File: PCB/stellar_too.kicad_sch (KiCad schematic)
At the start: 8 parts, among them J1 USB_C_Receptacle_USB2.0_14P, J2 USB_C_Receptacle_USB2.0_16P, U1 MDBT50Q, U2 FUSB302B01MPX

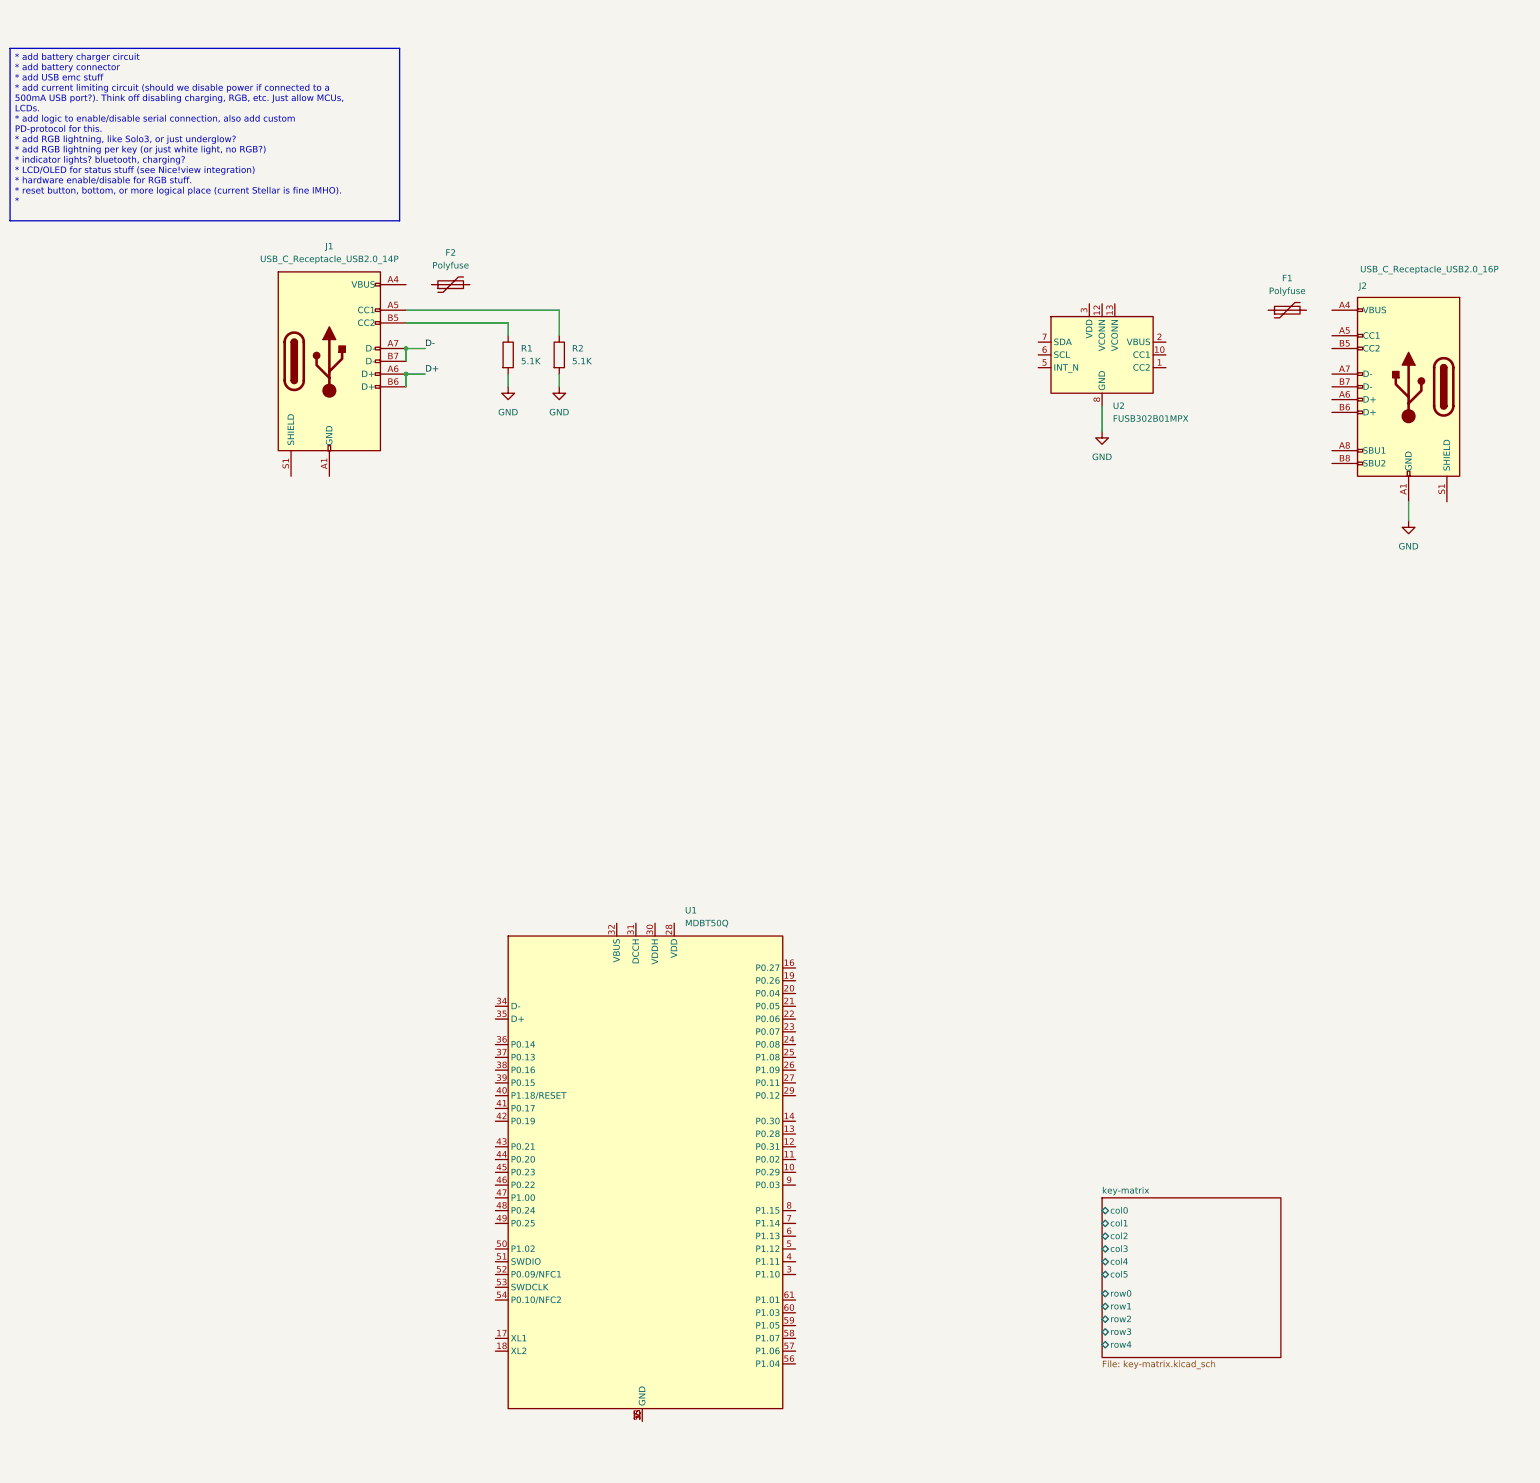
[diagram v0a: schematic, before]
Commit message: feat(pcb) layout of keys changed
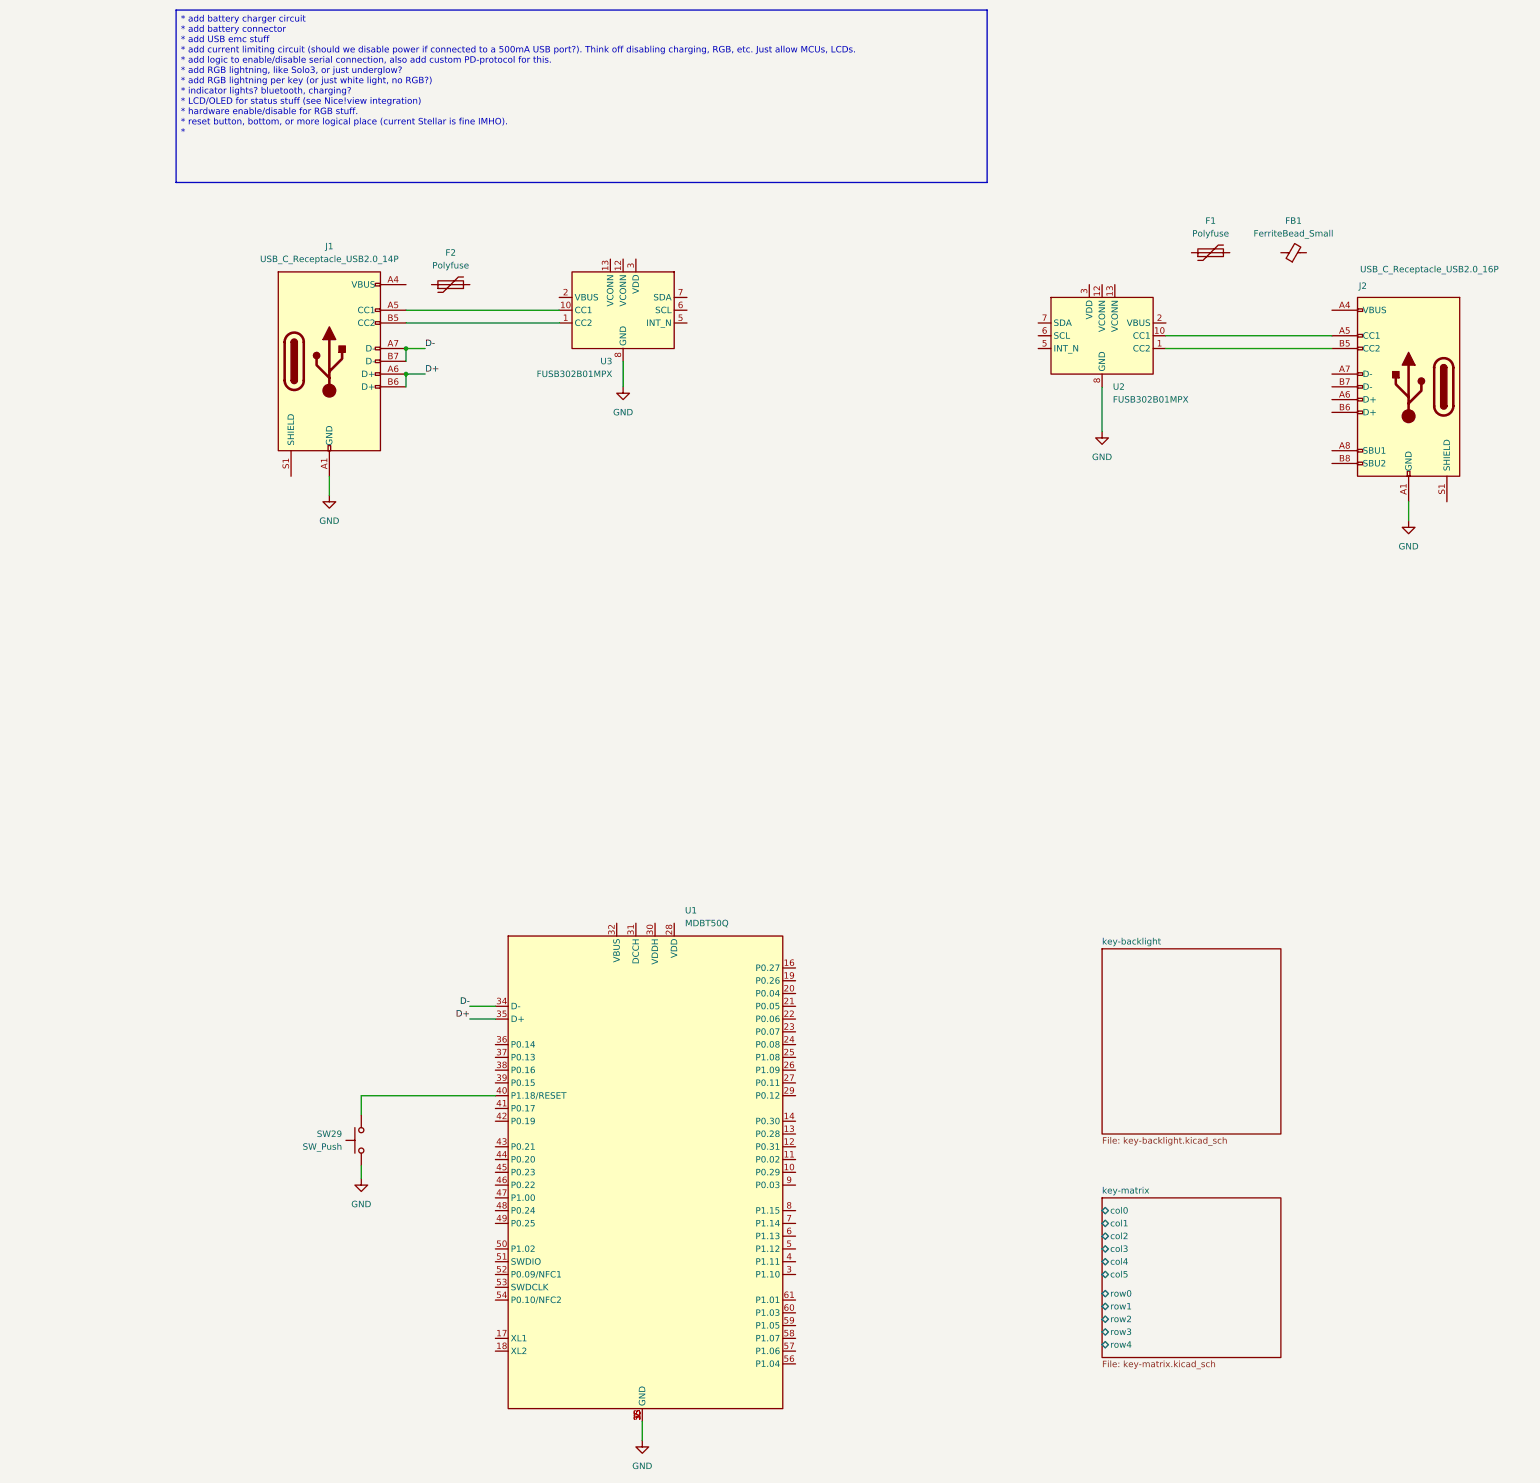
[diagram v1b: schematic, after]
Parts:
- removed R1, R2: 5.1K, symbol Device:R
- added FB1: FerriteBead_Small, symbol Device:FerriteBead_Small
- added SW29: SW_Push, symbol Switch:SW_Push
- added U3: FUSB302B01MPX, Package_DFN_QFN:WQFN-14-1EP_2.5x2.5mm_P0.5mm_EP1.45x1.45mm, symbol Interface_USB:FUSB302B01MPX
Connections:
- net D+: now also U1.35 (D+)
- net D-: now also U1.34 (D-)
- net GND: now also J1.A1 (GND), J1.A12 (GND), J1.B1 (GND), J1.B12 (GND), U1.1 (GND), U1.15 (GND), U1.2 (GND), U1.33 (GND), U1.55 (GND), SW29.2, U3.15 (GND), U3.8 (GND), U3.9 (GND)
- net at U1.40 (P1.18/RESET): now also SW29.1
- net at J1.A5 (CC1): now also U3.10 (CC1), U3.11 (CC1)
- net at J1.B5 (CC2): now also U3.1 (CC2), U3.14 (CC2)
- net at U2.1 (CC2), U2.14 (CC2): now also J2.B5 (CC2)
- net at U2.10 (CC1), U2.11 (CC1): now also J2.A5 (CC1)
- new net: U3.3 (VDD), U3.4 (VDD)
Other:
- added sheet key-backlight (key-backlight.kicad_sch)
- moved on the sheet: F1, U2

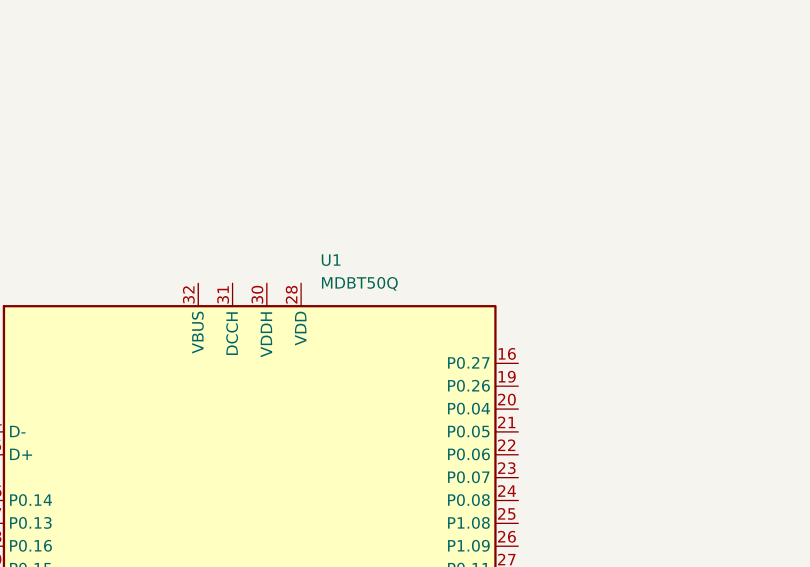
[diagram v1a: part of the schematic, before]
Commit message: feat(pcb) added e73-2g4m08s1c module
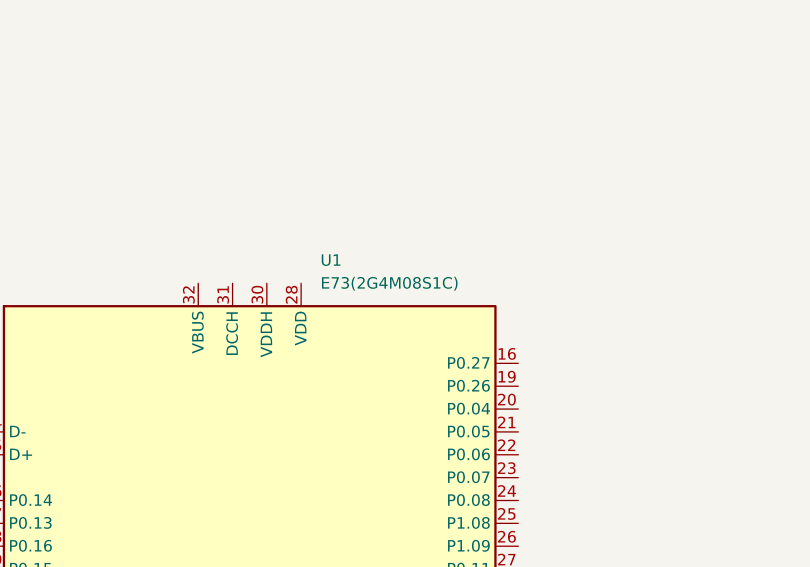
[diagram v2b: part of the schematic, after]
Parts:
- U1: value MDBT50Q -> E73(2G4M08S1C); footprint stellar:MDBT50Q -> stellar:E73(2G4M08S1C)
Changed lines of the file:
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@@
 			)
 		)
-		(property "Value" "MDBT50Q"
+		(property "Value" "E73(2G4M08S1C)"
 			(at 111.3633 157.48 0)
 			(effects
@@
 			)
 		)
-		(property "Footprint" "stellar:MDBT50Q"
+		(property "Footprint" "stellar:E73(2G4M08S1C)"
 			(at 76.2 160.02 0)
 			(effects

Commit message: feat(PCB) more wip
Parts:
- U1: footprint stellar:E73(2G4M08S1C) -> stellar:MDBT50Q
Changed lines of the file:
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@@
 			)
 		)
-		(property "Footprint" "stellar:E73(2G4M08S1C)"
+		(property "Footprint" "stellar:MDBT50Q"
 			(at 76.2 160.02 0)
 			(effects
